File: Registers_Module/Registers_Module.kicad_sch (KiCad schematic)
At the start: 1 part

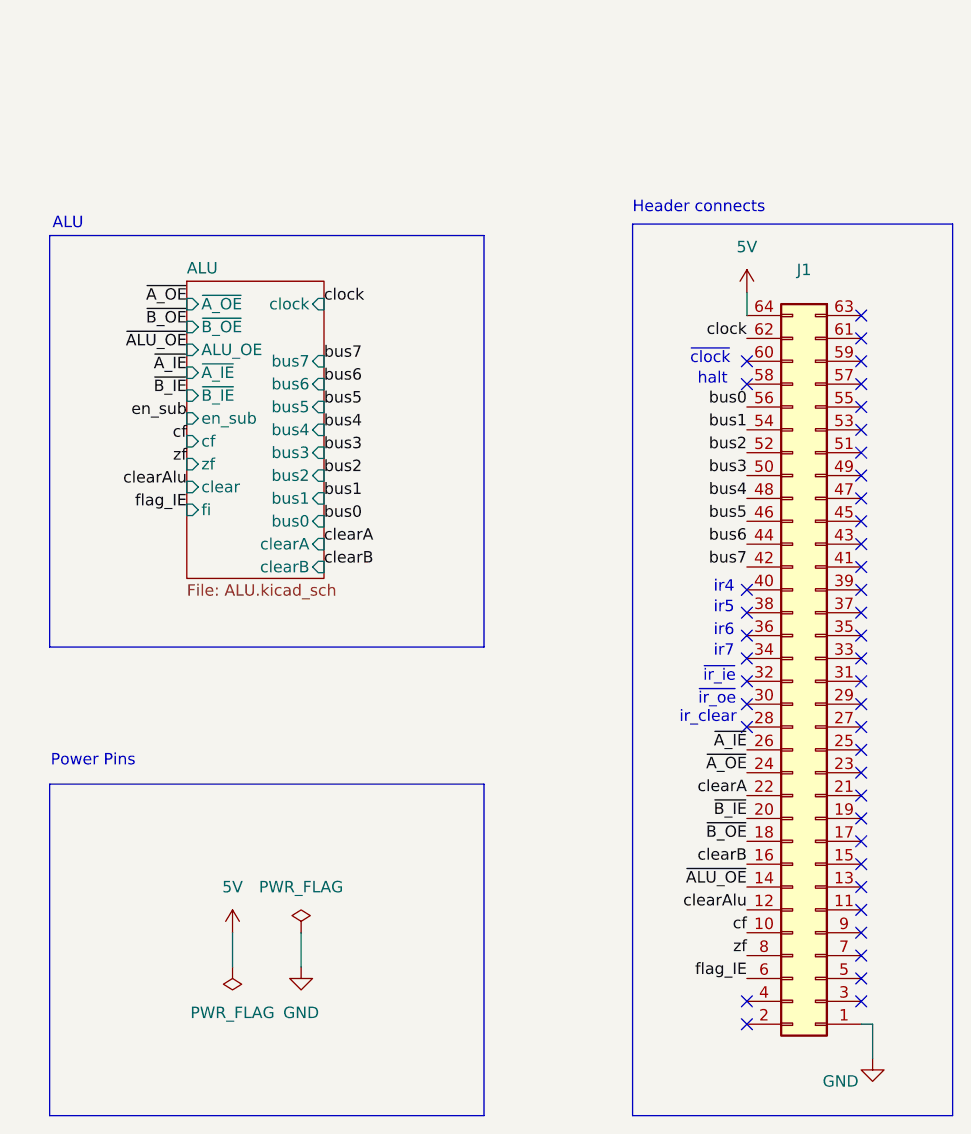
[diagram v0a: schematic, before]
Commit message: updated registers and alu
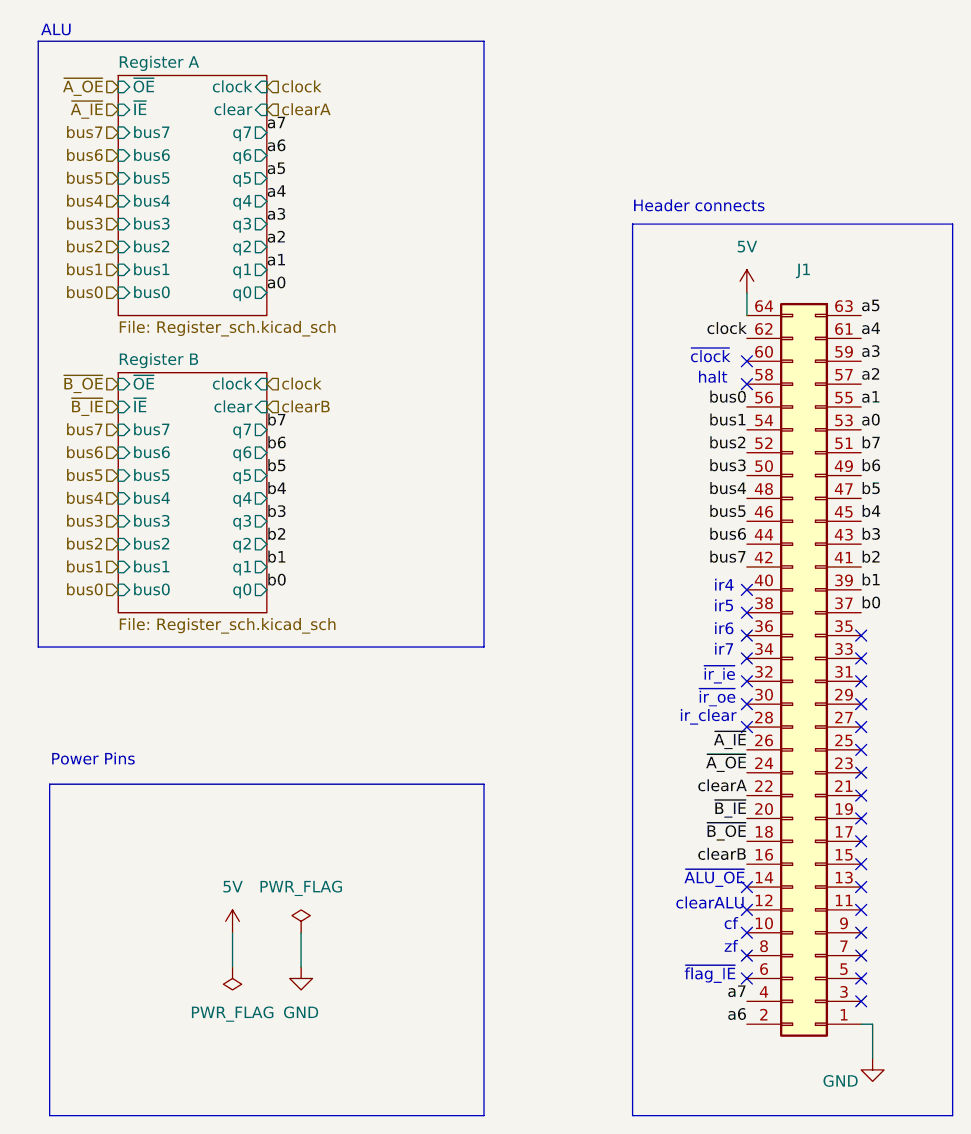
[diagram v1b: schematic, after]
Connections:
- net a6: now reaches J1.2
- net b0: now reaches J1.37
- net b1: now reaches J1.39
- net a7: now reaches J1.4
- net b2: now reaches J1.41
- net b3: now reaches J1.43
- net b4: now reaches J1.45
- net b5: now reaches J1.47
- net b6: now reaches J1.49
- net b7: now reaches J1.51
- net a0: now reaches J1.53
- net a1: now reaches J1.55
- net a2: now reaches J1.57
- net a3: now reaches J1.59
- net a4: now reaches J1.61
- net a5: now reaches J1.63
- net cf: no longer names the net of J1.10
- net clearAlu: no longer names the net of J1.12
- net flag_IE: no longer names the net of J1.6
- net zf: no longer names the net of J1.8
- net ~{ALU_OE}: no longer names the net of J1.14
- no-connect marks 42 -> 31
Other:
- removed sheet ALU
- added sheet Register A (Register_sch.kicad_sch)
- added sheet Register B (Register_sch.kicad_sch)
- note added: "cf"
- note added: "clearALU"
- note added: "zf"
- note added: "~{ALU_OE}"
- note added: "~{flag_IE}"

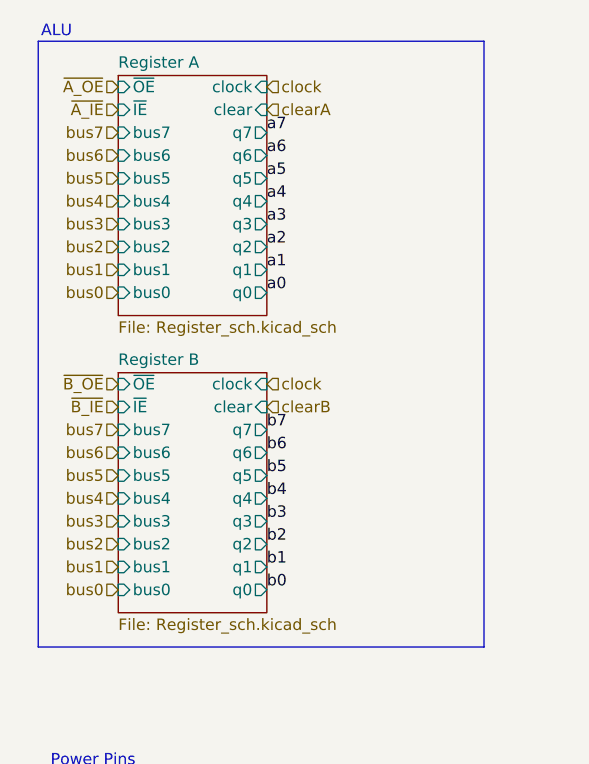
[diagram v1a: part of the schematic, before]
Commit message: merge and updates the Register module
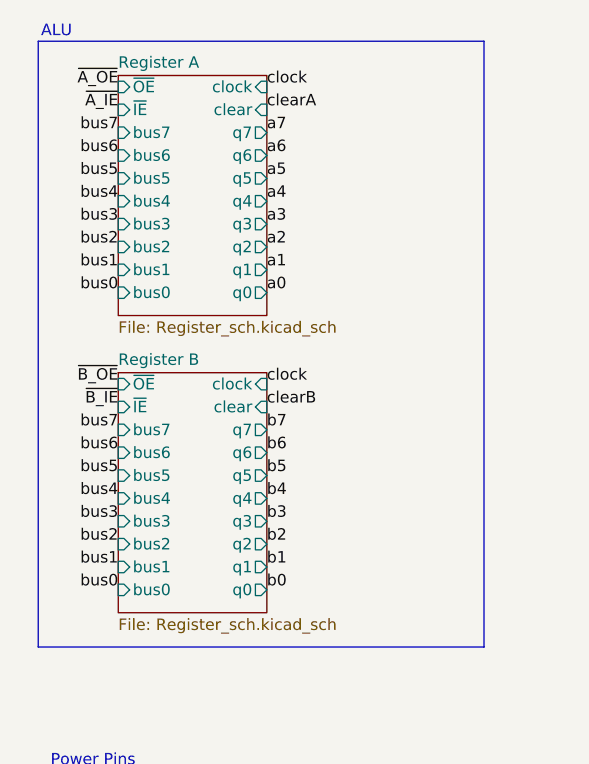
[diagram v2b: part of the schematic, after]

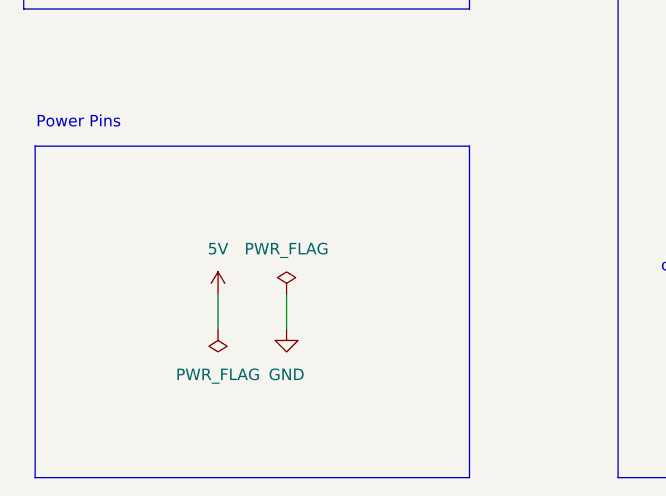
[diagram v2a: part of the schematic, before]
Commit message: added cap's between power pins
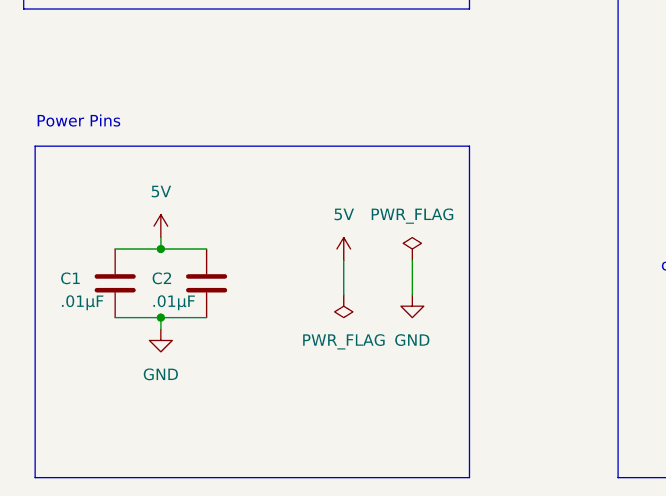
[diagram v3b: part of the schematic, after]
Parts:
- added C1, C2: .01µF, Capacitor_THT:C_Disc_D5.0mm_W2.5mm_P2.50mm, symbol Device:C
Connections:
- net 5V: now also C1.2, C2.2
- net GND: now also C1.1, C2.1

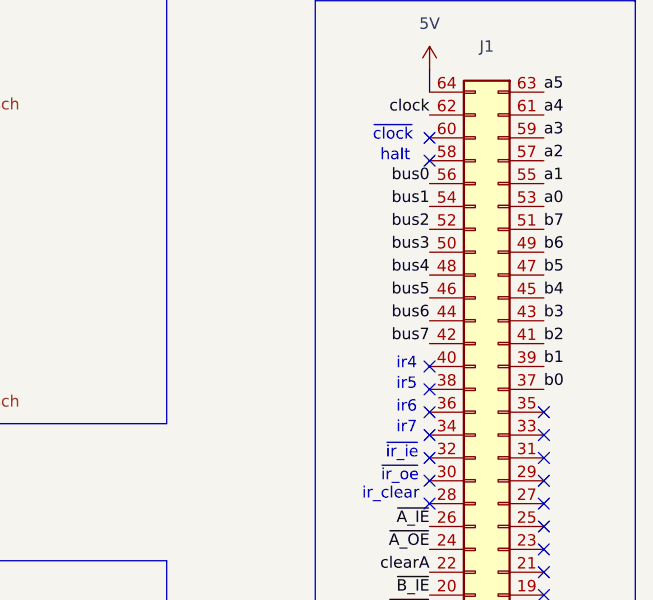
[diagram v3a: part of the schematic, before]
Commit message: updated RAM, changed bus alignment in ALU, RAM, and registers
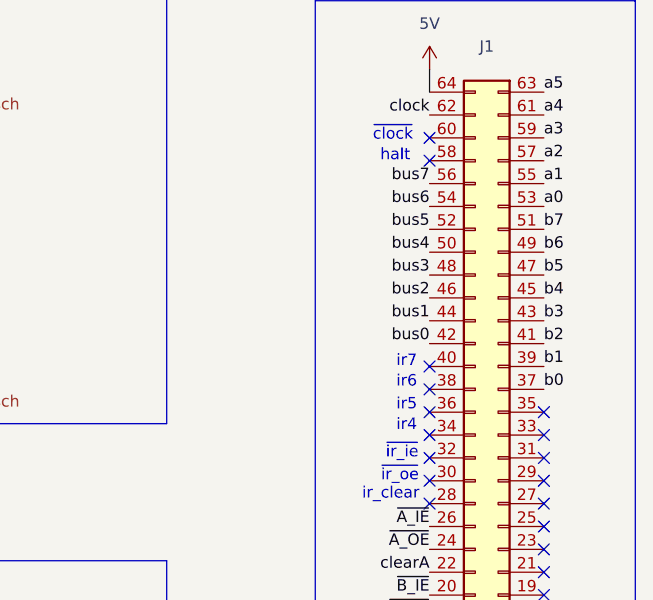
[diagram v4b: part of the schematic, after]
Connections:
- net bus0: now also J1.42; no longer J1.56
- net bus1: now also J1.44; no longer J1.54
- net bus2: now also J1.46; no longer J1.52
- net bus3: now also J1.48; no longer J1.50
- net bus4: now also J1.50; no longer J1.48
- net bus5: now also J1.52; no longer J1.46
- net bus6: now also J1.54; no longer J1.44
- net bus7: now also J1.56; no longer J1.42
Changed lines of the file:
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@@
 	(text "ir5"
 		(exclude_from_sim no)
-		(at 163.83 83.312 0)
+		(at 163.83 85.598 0)
 		(effects
 			(font
@@
 	(text "ir6"
 		(exclude_from_sim no)
-		(at 163.83 85.852 0)
+		(at 163.83 83.058 0)
 		(effects
 			(font
@@
 	(text "ir7"
 		(exclude_from_sim no)
-		(at 163.83 88.138 0)
+		(at 163.83 80.772 0)
 		(effects
 			(font
@@
 	(text "ir4"
 		(exclude_from_sim no)
-		(at 163.83 81.026 0)
+		(at 163.83 87.884 0)
 		(effects
 			(font
@@
 	)
 	(label "bus3"
+		(at 166.37 71.12 180)
+		(effects
+			(font
+				(size 1.27 1.27)
+			)
+			(justify right bottom)
+		)
+	)
+	(label "bus3"
 		(at 96.52 73.66 180)
 		(effects
@@
 		)
 	)
+	(label "bus6"
+		(at 166.37 63.5 180)
+		(effects
+			(font
+				(size 1.27 1.27)
+			)
+			(justify right bottom)
+		)
+	)
 	(label "b7"
 		(at 113.03 63.5 0)
@@
 		)
 	)
-	(label "bus5"
-		(at 166.37 73.66 180)
-		(effects
-			(font
-				(size 1.27 1.27)
-			)
-			(justify right bottom)
-		)
-	)
 	(label "bus6"
 		(at 96.52 66.04 180)
@@
 		)
 	)
+	(label "bus7"
+		(at 166.37 60.96 180)
+		(effects
+			(font
+				(size 1.27 1.27)
+			)
+			(justify right bottom)
+		)
+	)
 	(label "a5"
 		(at 113.03 35.56 0)
@@
 		)
 	)
+	(label "bus0"
+		(at 166.37 78.74 180)
+		(effects
+			(font
+				(size 1.27 1.27)
+			)
+			(justify right bottom)
+		)
+	)
 	(label "a1"
 		(at 113.03 45.72 0)
@@
 		)
 	)
-	(label "bus7"
-		(at 166.37 78.74 180)
+	(label "bus1"
+		(at 166.37 76.2 180)
 		(effects
 			(font
@@
 		)
 	)
+	(label "bus2"
+		(at 166.37 73.66 180)
+		(effects
+			(font
+				(size 1.27 1.27)
+			)
+			(justify right bottom)
+		)
+	)
 	(label "~{A_OE}"
 		(at 96.52 25.4 180)
@@
 		)
 	)
-	(label "bus4"
-		(at 166.37 71.12 180)
-		(effects
-			(font
-				(size 1.27 1.27)
-			)
-			(justify right bottom)
-		)
-	)
 	(label "a7"
 		(at 166.37 127 180)
@@
 		)
 	)
-	(label "bus3"
-		(at 166.37 68.58 180)
-		(effects
-			(font
-				(size 1.27 1.27)
-			)
-			(justify right bottom)
-		)
-	)
 	(label "b1"
 		(at 179.07 81.28 0)
@@
 		)
 	)
-	(label "bus1"
-		(at 166.37 63.5 180)
-		(effects
-			(font
-				(size 1.27 1.27)
-			)
-			(justify right bottom)
-		)
-	)
 	(label "clock"
 		(at 113.03 58.42 0)
@@
 		)
 	)
+	(label "bus5"
+		(at 166.37 66.04 180)
+		(effects
+			(font
+				(size 1.27 1.27)
+			)
+			(justify right bottom)
+		)
+	)
 	(label "b1"
 		(at 113.03 78.74 0)
@@
 		)
 	)
-	(label "bus6"
-		(at 166.37 76.2 180)
-		(effects
-			(font
-				(size 1.27 1.27)
-			)
-			(justify right bottom)
-		)
-	)
 	(label "b7"
 		(at 179.07 66.04 0)
@@
 		)
 	)
-	(label "bus0"
-		(at 166.37 60.96 180)
-		(effects
-			(font
-				(size 1.27 1.27)
-			)
-			(justify right bottom)
-		)
-	)
 	(label "b4"
 		(at 113.03 71.12 0)
@@
 		)
 	)
+	(label "bus4"
+		(at 166.37 68.58 180)
+		(effects
+			(font
+				(size 1.27 1.27)
+			)
+			(justify right bottom)
+		)
+	)
 	(label "b0"
 		(at 113.03 81.28 0)
@@
 		)
 	)
-	(label "bus2"
-		(at 166.37 66.04 180)
-		(effects
-			(font
-				(size 1.27 1.27)
-			)
-			(justify right bottom)
-		)
-	)
